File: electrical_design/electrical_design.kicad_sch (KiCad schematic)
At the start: 12 parts, among them M1 Left Motor, M2 Right Motor, U1 PIC24FJ64GA002-I/SP

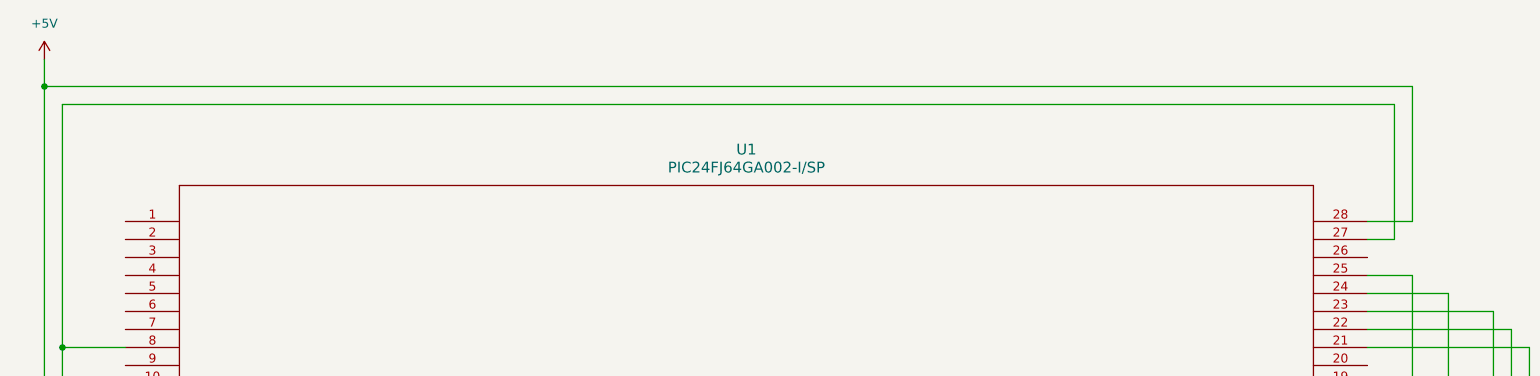
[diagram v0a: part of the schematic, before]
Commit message: Updated electrical and input capture for sensors
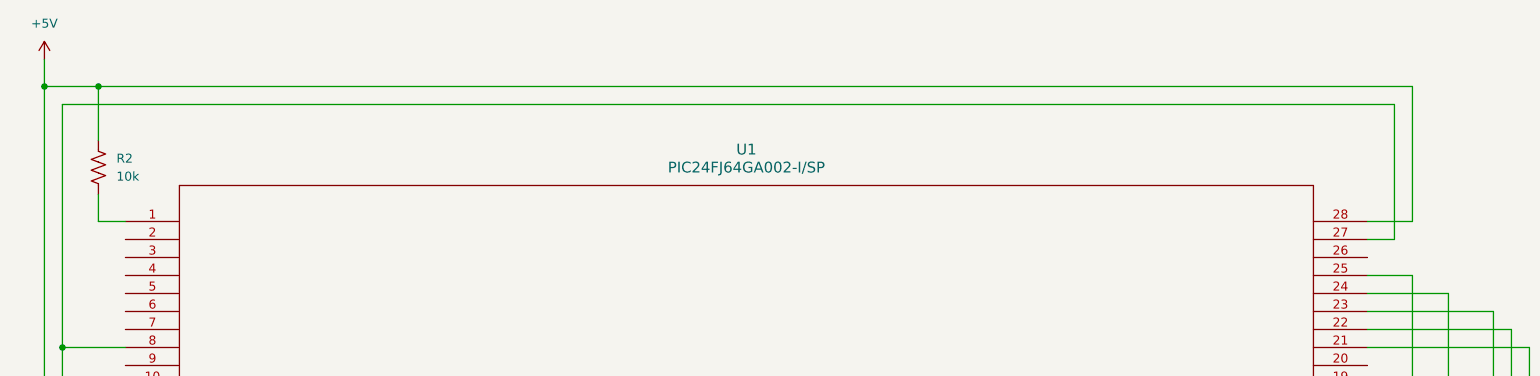
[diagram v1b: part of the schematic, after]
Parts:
- added R2: 10k, symbol Device:R_US
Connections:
- net +5V: now also R2.1
- net at U1.1: now also R2.2
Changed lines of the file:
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@@
+	)
+	(junction
+		(at 41.91 27.94)
+		(diameter 0)
+		(color 0 0 0 0)
 	)
 	(junction
@@
 	(wire
 		(pts
+			(xy 41.91 27.94) (xy 41.91 35.56)
+		)
+		(stroke
+			(width 0)
+			(type default)
+		)
+	)
+	(wire
+		(pts
 			(xy 59.69 105.41) (xy 59.69 139.7)
 		)
@@
 	(wire
 		(pts
-			(xy 34.29 27.94) (xy 227.33 27.94)
+			(xy 34.29 27.94) (xy 41.91 27.94)
+		)
+		(stroke
+			(width 0)
+			(type default)
+		)
+	)
+	(wire
+		(pts
+			(xy 41.91 27.94) (xy 227.33 27.94)
 		)
 		(stroke
@@
 	(wire
 		(pts
+			(xy 41.91 46.99) (xy 41.91 43.18)
+		)
+		(stroke
+			(width 0)
+			(type default)
+		)
+	)
+	(wire
+		(pts
 			(xy 59.69 139.7) (xy 224.79 139.7)
 		)
@@
 		(pts
 			(xy 106.68 102.87) (xy 111.76 102.87)
+		)
+		(stroke
+			(width 0)
+			(type default)
+		)
+	)
+	(wire
+		(pts
+			(xy 45.72 46.99) (xy 41.91 46.99)
 		)
 		(stroke
@@
 					(unit 1)
 				)
+			)
+		)
+	)
+	(symbol
+		(lib_id "Device:R_US")
+		(at 41.91 39.37 0)
+		(unit 1)
+		(body_style 1)
+		(exclude_from_sim no)
+		(in_bom yes)
+		(on_board yes)
+		(in_pos_files yes)
+		(dnp no)
+		(fields_autoplaced yes)
+		(property "Reference" "R2"
+			(at 44.45 38.0999 0)
+			(show_name no)
+			(do_not_autoplace no)
+			(effects
+				(font
+					(size 1.27 1.27)
+				)
+				(justify left)
+			)
+		)
+		(property "Value" "10k"
+			(at 44.45 40.6399 0)
+			(show_name no)
+			(do_not_autoplace no)
+			(effects
+				(font
+					(size 1.27 1.27)
+				)
+				(justify left)
+			)
+		)
+		(property "Footprint" ""
+			(at 42.926 39.624 90)
+			(hide yes)
+			(show_name no)
+			(do_not_autoplace no)
+			(effects
+				(font
+					(size 1.27 1.27)
+				)
+			)
+		)
+		(property "Datasheet" ""
+			(at 41.91 39.37 0)
+			(hide yes)
+			(show_name no)
+			(do_not_autoplace no)
+			(effects
+				(font
+					(size 1.27 1.27)
+				)
+			)
+		)
+		(property "Description" "Resistor, US symbol"
+			(at 41.91 39.37 0)
+			(hide yes)
+			(show_name no)
+			(do_not_autoplace no)
+			(effects
+				(font
+					(size 1.27 1.27)
+				)
+			)
+		)
+		(pin "1"
+		)
+		(pin "2"
+		)
+		(instances
+			(project "electrical_design"
+				(path "/3686bf86-00d7-4374-9d73-095afbe73533"
+					(reference "R2")
+					(unit 1)
+				)

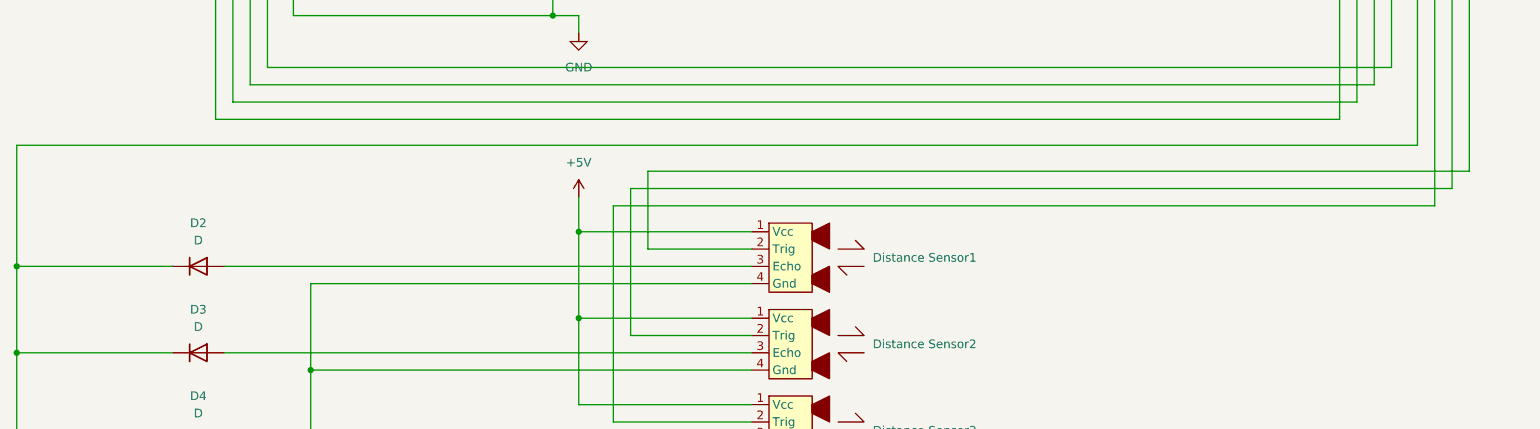
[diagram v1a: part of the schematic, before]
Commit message: Pull-down resistor on ECHO input and bug fixes
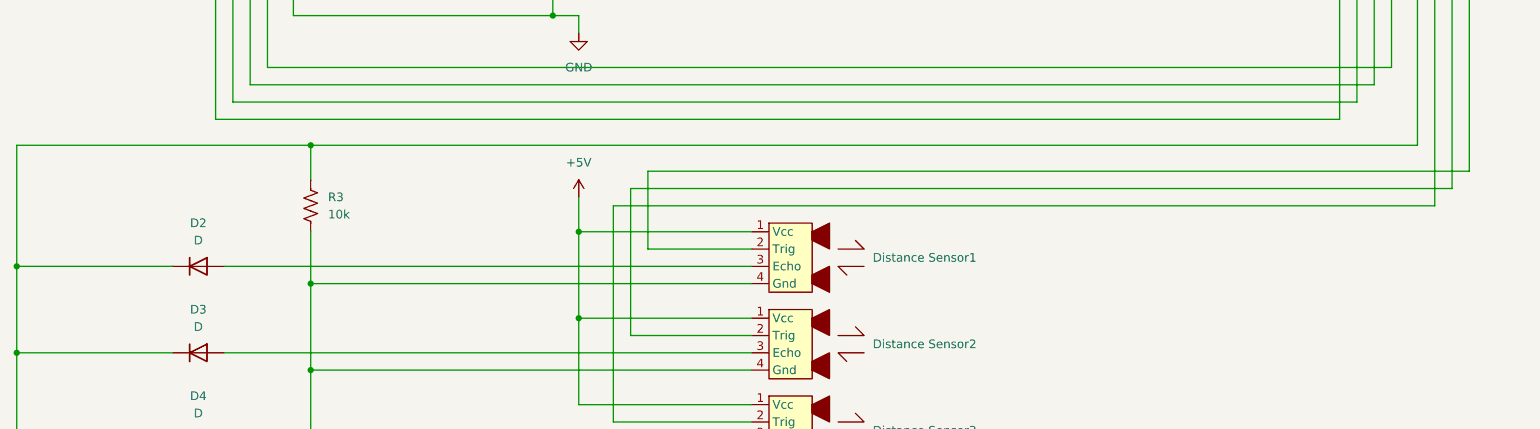
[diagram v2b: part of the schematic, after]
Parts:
- added R3: 10k, symbol Device:R_US
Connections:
- net GND: now also R3.2
- net at D2.1 (K), D3.1 (K), D4.1 (K)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: now also R3.1
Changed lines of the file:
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@@
+	)
+	(junction
+		(at 73.66 163.83)
+		(diameter 0)
+		(color 0 0 0 0)
 	)
 	(junction
@@
 	)
 	(junction
+		(at 73.66 143.51)
+		(diameter 0)
+		(color 0 0 0 0)
+	)
+	(junction
 		(at 36.83 64.77)
 		(diameter 0)
@@
 	(wire
 		(pts
-			(xy 30.48 143.51) (xy 236.22 143.51)
+			(xy 30.48 143.51) (xy 73.66 143.51)
 		)
 		(stroke
@@
 	(wire
 		(pts
+			(xy 73.66 156.21) (xy 73.66 163.83)
+		)
+		(stroke
+			(width 0)
+			(type default)
+		)
+	)
+	(wire
+		(pts
 			(xy 138.43 176.53) (xy 73.66 176.53)
 		)
@@
 	(wire
 		(pts
+			(xy 73.66 143.51) (xy 236.22 143.51)
+		)
+		(stroke
+			(width 0)
+			(type default)
+		)
+	)
+	(wire
+		(pts
 			(xy 73.66 115.57) (xy 68.58 115.57)
 		)
@@
 		(pts
 			(xy 224.79 80.01) (xy 220.98 80.01)
+		)
+		(stroke
+			(width 0)
+			(type default)
+		)
+	)
+	(wire
+		(pts
+			(xy 73.66 143.51) (xy 73.66 148.59)
 		)
 		(stroke
@@
 					(unit 1)
 				)
+			)
+		)
+	)
+	(symbol
+		(lib_id "Device:R_US")
+		(at 73.66 152.4 0)
+		(unit 1)
+		(body_style 1)
+		(exclude_from_sim no)
+		(in_bom yes)
+		(on_board yes)
+		(in_pos_files yes)
+		(dnp no)
+		(fields_autoplaced yes)
+		(property "Reference" "R3"
+			(at 76.2 151.1299 0)
+			(show_name no)
+			(do_not_autoplace no)
+			(effects
+				(font
+					(size 1.27 1.27)
+				)
+				(justify left)
+			)
+		)
+		(property "Value" "10k"
+			(at 76.2 153.6699 0)
+			(show_name no)
+			(do_not_autoplace no)
+			(effects
+				(font
+					(size 1.27 1.27)
+				)
+				(justify left)
+			)
+		)
+		(property "Footprint" ""
+			(at 74.676 152.654 90)
+			(hide yes)
+			(show_name no)
+			(do_not_autoplace no)
+			(effects
+				(font
+					(size 1.27 1.27)
+				)
+			)
+		)
+		(property "Datasheet" ""
+			(at 73.66 152.4 0)
+			(hide yes)
+			(show_name no)
+			(do_not_autoplace no)
+			(effects
+				(font
+					(size 1.27 1.27)
+				)
+			)
+		)
+		(property "Description" "Resistor, US symbol"
+			(at 73.66 152.4 0)
+			(hide yes)
+			(show_name no)
+			(do_not_autoplace no)
+			(effects
+				(font
+					(size 1.27 1.27)
+				)
+			)
+		)
+		(pin "1"
+		)
+		(pin "2"
+		)
+		(instances
+			(project "electrical_design"
+				(path "/3686bf86-00d7-4374-9d73-095afbe73533"
+					(reference "R3")
+					(unit 1)
+				)

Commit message: KiCAD Footprints
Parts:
- Motor Controller1: footprint (none) -> Package_DIP:DIP-14_W7.62mm
- U1: footprint SPDIP28_300MC_MCH -> Package_DIP:DIP-28_W7.62mm_Socket
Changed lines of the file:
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@@
 			)
 		)
-		(property "Footprint" ""
+		(property "Footprint" "Package_DIP:DIP-14_W7.62mm"
 			(at 90.17 104.14 0)
 			(hide yes)
@@
 			)
 		)
-		(property "Footprint" "SPDIP28_300MC_MCH"
+		(property "Footprint" "Package_DIP:DIP-28_W7.62mm_Socket"
 			(at 45.72 46.99 0)
 			(hide yes)

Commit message: Working corrective actions
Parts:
- added J1: Conn_01x02_Pin, Connector_PinHeader_2.54mm:PinHeader_1x02_P2.54mm_Vertical, symbol Connector:Conn_01x02_Pin
- D1: footprint (none) -> LED_THT:LED_D5.0mm
- D2, D3, D4: footprint (none) -> Diode_THT:D_A-405_P7.62mm_Horizontal
- Distance Sensor1: footprint (none) -> Connector_PinHeader_2.54mm:PinHeader_1x04_P2.54mm_Vertical
- Distance Sensor2: footprint (none) -> Connector_PinHeader_2.54mm:PinHeader_1x04_P2.54mm_Vertical
- Distance Sensor3: footprint (none) -> Connector_PinHeader_2.54mm:PinHeader_1x04_P2.54mm_Vertical
- M1, M2: footprint (none) -> Connector_PinHeader_2.54mm:PinHeader_1x02_P2.54mm_Vertical
- R1, R2, R3: footprint (none) -> Resistor_THT:R_Axial_DIN0204_L3.6mm_D1.6mm_P7.62mm_Horizontal
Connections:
- net +5V: now also J1.1 (Pin_1)
- net GND: now also J1.2 (Pin_2)
